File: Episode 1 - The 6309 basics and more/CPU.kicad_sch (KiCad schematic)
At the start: 34 parts, among them Q1 PN2222, SW1 Reset, U1 74AHCT541, U2 74AHCT245, U3 HD63C09, U4 74AHCT541, U5 74AHCT541, U6 ATF750C, U7 LMC555, Y1 16 MHz

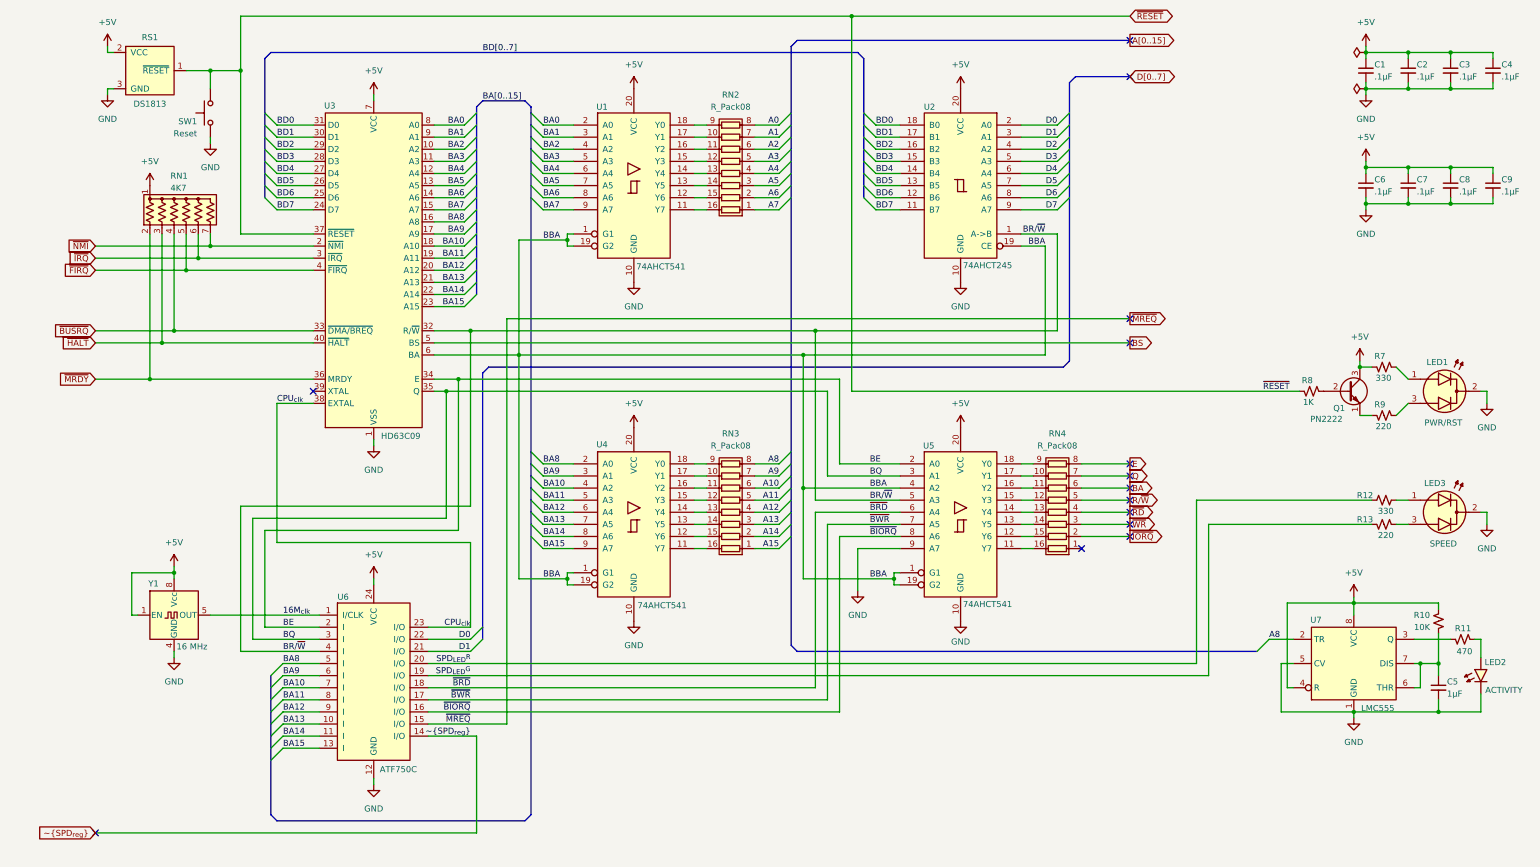
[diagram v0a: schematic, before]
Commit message: Updating PCB option
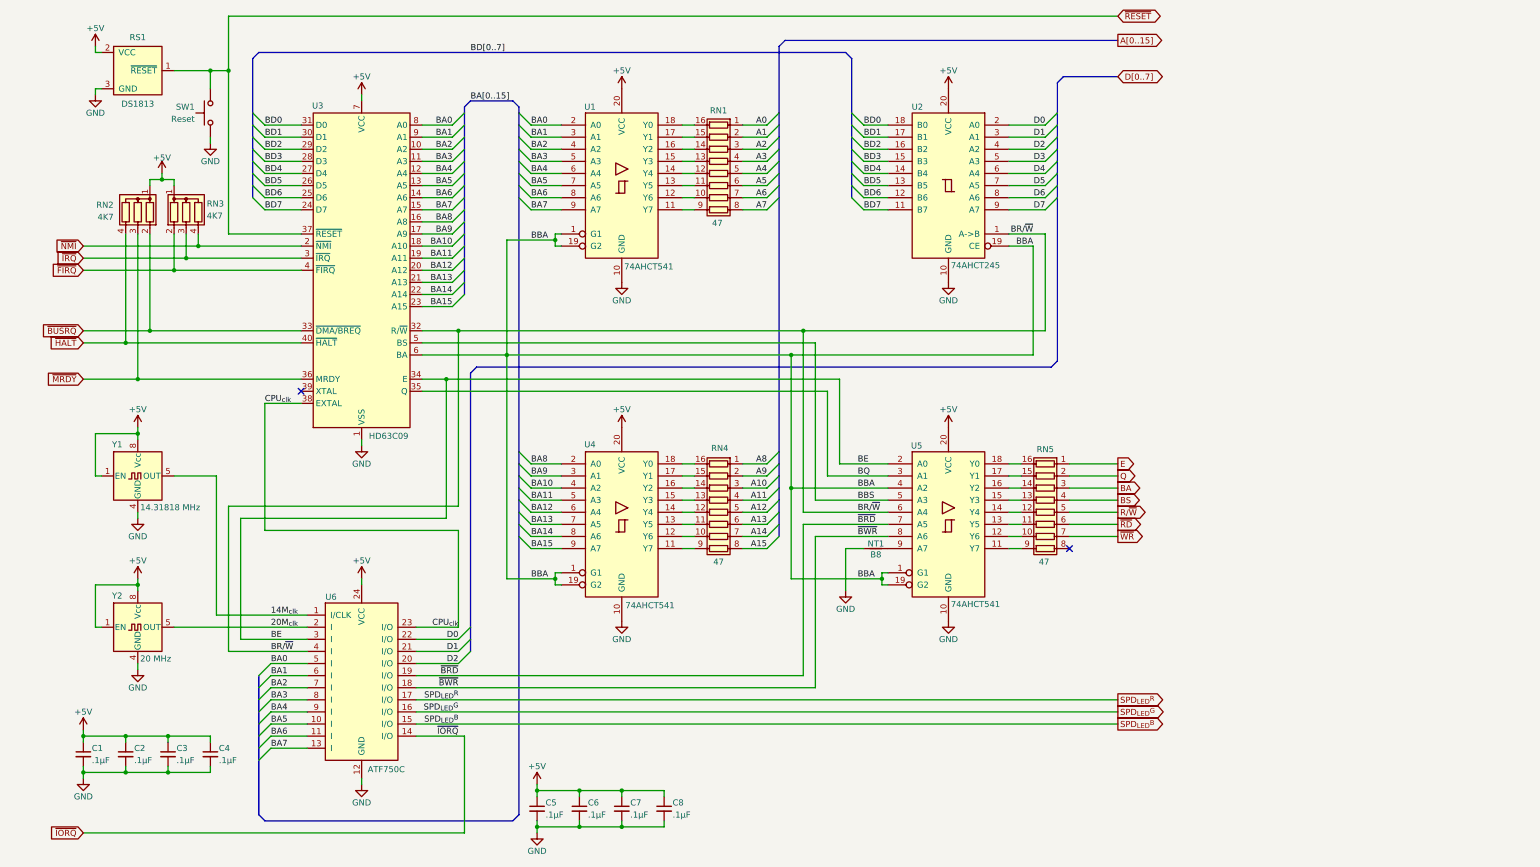
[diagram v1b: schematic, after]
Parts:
- removed C5: 1µF, Capacitor_THT:C_Disc_D3.0mm_W1.6mm_P2.50mm, symbol Device:C_Small
- removed C9: .1µF, Capacitor_THT:C_Disc_D3.0mm_W1.6mm_P2.50mm, symbol Device:C_Small
- removed LED1: PWR/RST, PCM_LED_THT_AKL:LED_D3.0mm-3_CC, symbol PCM_LED_AKL:LED_3mm_Kcom_Red_Green
- removed LED2: ACTIVITY, PCM_LED_THT_AKL:LED_D3.0mm, symbol PCM_LED_AKL:LED_3mm_Blue
- removed LED3: SPEED, PCM_LED_THT_AKL:LED_D3.0mm-3_CC, symbol PCM_LED_AKL:LED_3mm_Kcom_Red_Green
- removed Q1: PN2222, Package_TO_SOT_THT:TO-92_Inline, symbol Transistor_BJT:PN2222A
- removed R10: 10K, Resistor_THT:R_Axial_DIN0204_L3.6mm_D1.6mm_P7.62mm_Horizontal, symbol Device:R_Small_US
- removed R11: 470, Resistor_THT:R_Axial_DIN0204_L3.6mm_D1.6mm_P7.62mm_Horizontal, symbol Device:R_Small_US
- removed R12, R7: 330, Resistor_THT:R_Axial_DIN0204_L3.6mm_D1.6mm_P7.62mm_Horizontal, symbol Device:R_Small_US
- removed R13, R9: 220, Resistor_THT:R_Axial_DIN0204_L3.6mm_D1.6mm_P7.62mm_Horizontal, symbol Device:R_Small_US
- removed R8: 1K, Resistor_THT:R_Axial_DIN0204_L3.6mm_D1.6mm_P7.62mm_Horizontal, symbol Device:R_Small_US
- removed RN1: 4K7, Resistor_THT:R_Array_SIP7, symbol Device:R_Network06_US
- removed U7: LMC555, Package_DIP:DIP-8_W7.62mm_Socket, symbol Timer:LMC555xN
- added C8: .1µF, Capacitor_THT:C_Disc_D3.0mm_W1.6mm_P2.50mm, symbol Device:C_Small
- added NT1: B8, Jumper:SolderJumper-2_P1.3mm_Bridged_RoundedPad1.0x1.5mm, symbol Device:NetTie_2
- added RN2, RN3: 4K7, Resistor_THT:R_Array_SIP4, symbol Device:R_Network03
- added Y2: 20 MHz, Oscillator:Oscillator_DIP-8, symbol Oscillator:CXO_DIP8
- RN1: renamed from RN2; value R_Pack08 -> 47; footprint (none) -> Package_DIP:DIP-16_W7.62mm_Socket
- RN4: renamed from RN3; value R_Pack08 -> 47; footprint (none) -> Package_DIP:DIP-16_W7.62mm_Socket
- RN5: renamed from RN4; value R_Pack08 -> 47; footprint (none) -> Package_DIP:DIP-16_W7.62mm_Socket
- Y1: value 16 MHz -> 14.31818 MHz
- renumbered C6 to C5, C7 to C6, C8 to C7
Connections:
- net ~{SPD_{reg}} is gone; now on net ~{IORQ}: U6.14 (I/O)
- net +5V: now also C8.1, RN2.1 (common), RN3.1 (common), Y2.1 (EN), Y2.8 (Vcc)
- net A0: now also RN1.1 (R1.1); no longer RN1.8 (R8.1)
- net A1: now also RN1.2 (R2.1); no longer RN1.7 (R7.1)
- net A10: now also RN4.3 (R3.1); no longer RN4.6 (R6.1)
- net A11: now also RN4.4 (R4.1); no longer RN4.5 (R5.1)
- net A12: now also RN4.5 (R5.1); no longer RN4.4 (R4.1)
- net A13: now also RN4.6 (R6.1); no longer RN4.3 (R3.1)
- net A14: now also RN4.7 (R7.1); no longer RN4.2 (R2.1)
- net A15: now also RN4.8 (R8.1); no longer RN4.1 (R1.1)
- net A2: now also RN1.3 (R3.1); no longer RN1.6 (R6.1)
- net A3: now also RN1.4 (R4.1); no longer RN1.5 (R5.1)
- net A4: now also RN1.5 (R5.1); no longer RN1.4 (R4.1)
- net A5: now also RN1.6 (R6.1); no longer RN1.3 (R3.1)
- net A6: now also RN1.7 (R7.1); no longer RN1.2 (R2.1)
- net A7: now also RN1.8 (R8.1); no longer RN1.1 (R1.1)
- net A8: now also RN4.1 (R1.1); no longer RN4.8 (R8.1)
- net A9: now also RN4.2 (R2.1); no longer RN4.7 (R7.1)
- net BA: now also RN5.3 (R3.1); no longer RN5.6 (R6.1)
- net BA0: now also U6.5 (I)
- net BA1: now also U6.6 (I)
- net BA10: no longer U6.7 (I)
- net BA11: no longer U6.8 (I)
- net BA12: no longer U6.9 (I)
- net BA13: no longer U6.10 (I)
- net BA14: no longer U6.11 (I)
- net BA15: no longer U6.13 (I)
- net BA2: now also U6.7 (I)
- net BA3: now also U6.8 (I)
- net BA4: now also U6.9 (I)
- net BA5: now also U6.10 (I)
- net BA6: now also U6.11 (I)
- net BA7: now also U6.13 (I)
- net BA8: no longer U6.5 (I)
- net BA9: no longer U6.6 (I)
- net BE: now also U6.3 (I); no longer U6.2 (I)
- net BQ: no longer U6.3 (I)
- net BR/~{W}: now also U5.6 (A4); no longer U5.5 (A3)
- net BS: now also RN5.4 (R4.1); no longer U3.5 (BS)
- net D2: now also U6.20 (I/O)
- net E: now also RN5.1 (R1.1); no longer RN5.8 (R8.1)
- net GND: now also C8.2, NT1.1, Y2.4 (GND); no longer U5.9 (A7)
- net Q: now also RN5.2 (R2.1); no longer RN5.7 (R7.1)
- net SPD_{LED}^{G}: now also U6.16 (I/O); no longer U6.19 (I/O)
- net SPD_{LED}^{R}: now also U6.17 (I/O); no longer U6.20 (I/O)
- net ~{BRD}: now also U5.7 (A5), U6.19 (I/O); no longer U5.6 (A4), U6.18 (I/O)
- net ~{BUSRQ}: now also RN2.2 (R1)
- net ~{BWR}: now also U5.8 (A6), U6.18 (I/O); no longer U5.7 (A5), U6.17 (I/O)
- net ~{FIRQ}: now also RN3.2 (R1)
- net ~{HALT}: now also RN2.4 (R3)
- net ~{IORQ}: no longer RN5.2 (R2.1)
- net ~{IRQ}: now also RN3.3 (R2)
- net ~{MRDY}: now also RN2.3 (R2)
- net ~{NMI}: now also RN3.4 (R3)
- net ~{RD}: now also RN5.6 (R6.1); no longer RN5.4 (R4.1)
- net ~{WR}: now also RN5.7 (R7.1); no longer RN5.3 (R3.1)
- net at U4.11 (Y7): now also RN4.9 (R8.2); no longer RN4.16 (R1.2)
- net at U4.12 (Y6): now also RN4.10 (R7.2); no longer RN4.15 (R2.2)
- net at U4.13 (Y5): now also RN4.11 (R6.2); no longer RN4.14 (R3.2)
- net at U4.14 (Y4): now also RN4.12 (R5.2); no longer RN4.13 (R4.2)
- net at U4.15 (Y3): now also RN4.13 (R4.2); no longer RN4.12 (R5.2)
- net at U4.16 (Y2): now also RN4.14 (R3.2); no longer RN4.11 (R6.2)
- net at U4.17 (Y1): now also RN4.15 (R2.2); no longer RN4.10 (R7.2)
- net at U4.18 (Y0): now also RN4.16 (R1.2); no longer RN4.9 (R8.2)
- net at U5.11 (Y7): now also RN5.9 (R8.2); no longer RN5.16 (R1.2)
- net at U5.12 (Y6): now also RN5.10 (R7.2); no longer RN5.15 (R2.2)
- net at U5.13 (Y5): now also RN5.11 (R6.2); no longer RN5.14 (R3.2)
- net at U5.14 (Y4): now also RN5.12 (R5.2); no longer RN5.13 (R4.2)
- net at U5.15 (Y3): now also RN5.13 (R4.2); no longer RN5.12 (R5.2)
- net at U5.16 (Y2): now also RN5.14 (R3.2); no longer RN5.11 (R6.2)
- net at U5.17 (Y1): now also RN5.15 (R2.2); no longer RN5.10 (R7.2)
- net at U5.18 (Y0): now also RN5.16 (R1.2); no longer RN5.9 (R8.2)
- net at U1.11 (Y7): now also RN1.9 (R8.2); no longer RN1.16 (R1.2)
- net at U1.12 (Y6): now also RN1.10 (R7.2); no longer RN1.15 (R2.2)
- net at U1.13 (Y5): now also RN1.11 (R6.2); no longer RN1.14 (R3.2)
- net at U1.14 (Y4): now also RN1.12 (R5.2); no longer RN1.13 (R4.2)
- net at U1.15 (Y3): now also RN1.13 (R4.2); no longer RN1.12 (R5.2)
- net at U1.16 (Y2): now also RN1.14 (R3.2); no longer RN1.11 (R6.2)
- net at U1.17 (Y1): now also RN1.15 (R2.2); no longer RN1.10 (R7.2)
- net at U1.18 (Y0): now also RN1.16 (R1.2); no longer RN1.9 (R8.2)
- net 16M_{clk} renamed 14M_{clk}
- removed net ~{BIORQ}: U5.8 (A6), U6.16 (I/O)
- net ~{MREQ} renamed SPD_{LED}^{B}
- new net: NT1.2, U5.9 (A7)
- new net 20M_{clk}: U6.2 (I), Y2.5 (OUT)
- new net BBS: U3.5 (BS), U5.5 (A3)
- no-connect marks 14 -> 2
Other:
- moved on the sheet: C1, C2, C3, C4, C5, C6, C7, RN1, RN4, RN5, RS1, U1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
